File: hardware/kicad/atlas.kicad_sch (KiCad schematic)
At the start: 0 parts

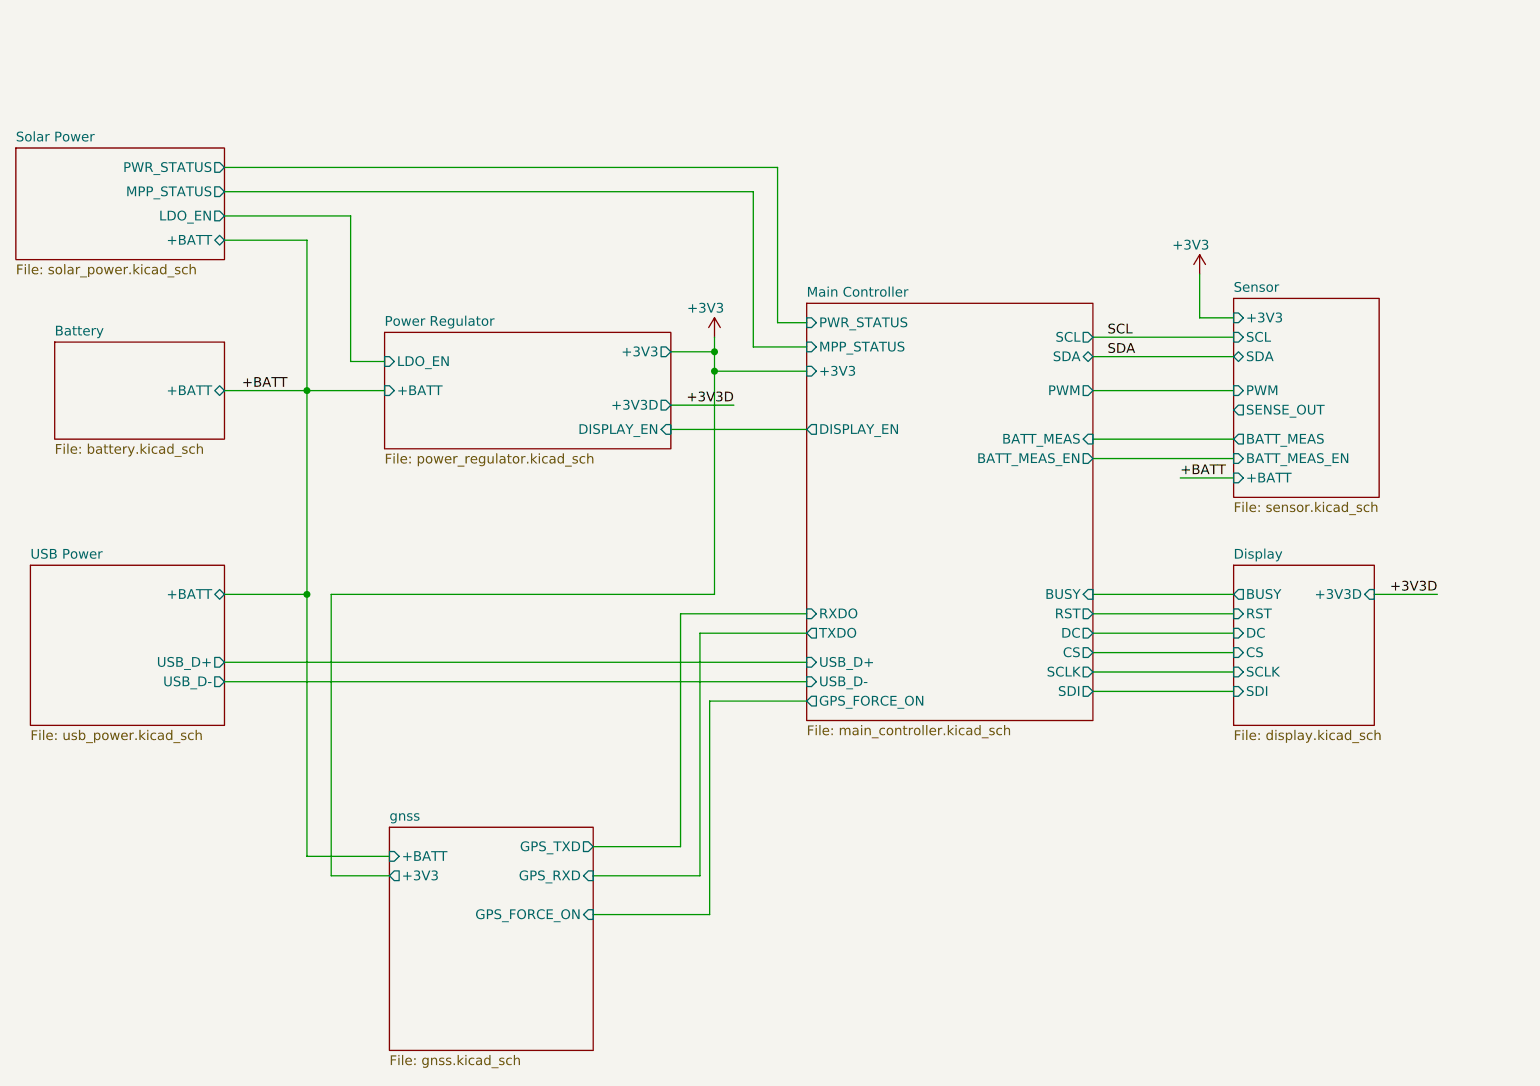
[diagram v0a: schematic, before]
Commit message: update schematics with gnss
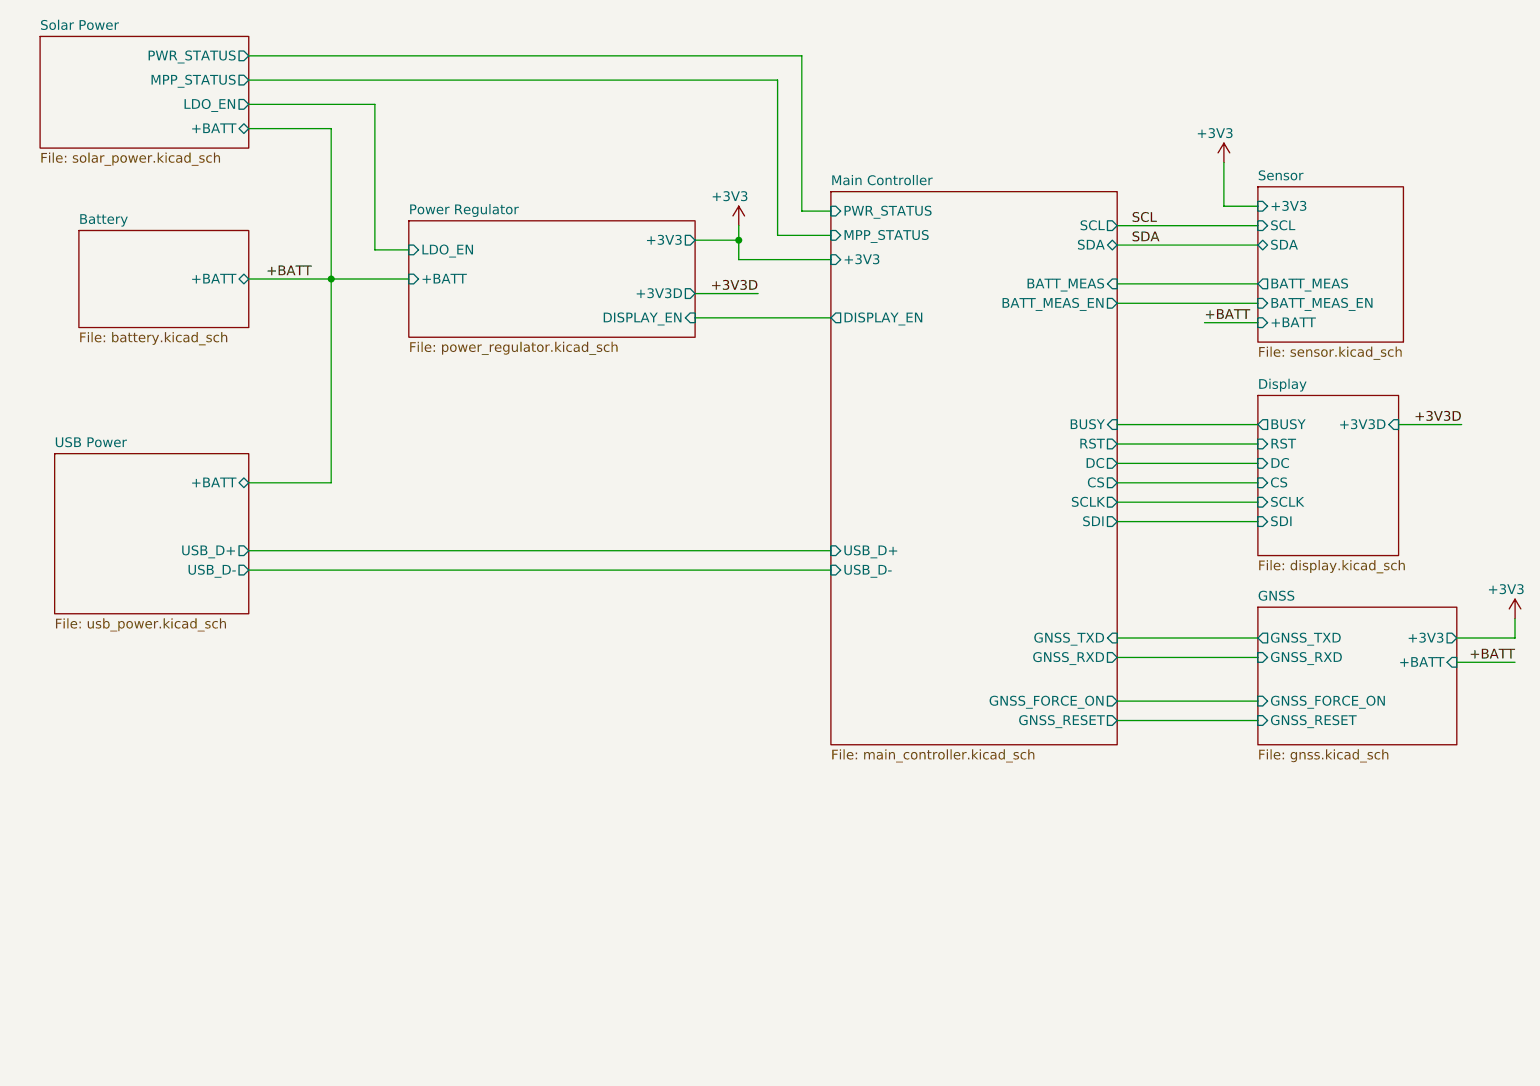
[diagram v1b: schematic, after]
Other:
- sheet gnss renamed GNSS
- sheet GNSS ports: added GNSS_FORCE_ON, GNSS_RESET, GNSS_RXD, GNSS_TXD; removed GPS_FORCE_ON, GPS_RXD, GPS_TXD
- sheet Main Controller ports: added GNSS_FORCE_ON, GNSS_RESET, GNSS_RXD, GNSS_TXD; removed GPS_FORCE_ON, PWM, RXDO, TXDO
- sheet Sensor ports: added none; removed PWM, SENSE_OUT

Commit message: update schematics info
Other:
- title: Teapotlabs Plantpal -> Teapotlabs Atlas
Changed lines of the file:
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@@
 	(paper "A4")
 	(title_block
-		(title "Teapotlabs Plantpal")
-		(date "2024-04-06")
-		(rev "5")
+		(title "Teapotlabs Atlas")
+		(date "2024-10-25")
+		(rev "1")
 		(company "Teapot Laboratories")
 	)
